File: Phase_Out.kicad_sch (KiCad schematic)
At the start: 34 parts, among them Q1 CLAMP_FET, Q2 CLAMP_FET, Q3 CLAMP_FET, Q4 CLAMP_FET, Q5 CLAMP_FET, Q6 CLAMP_FET

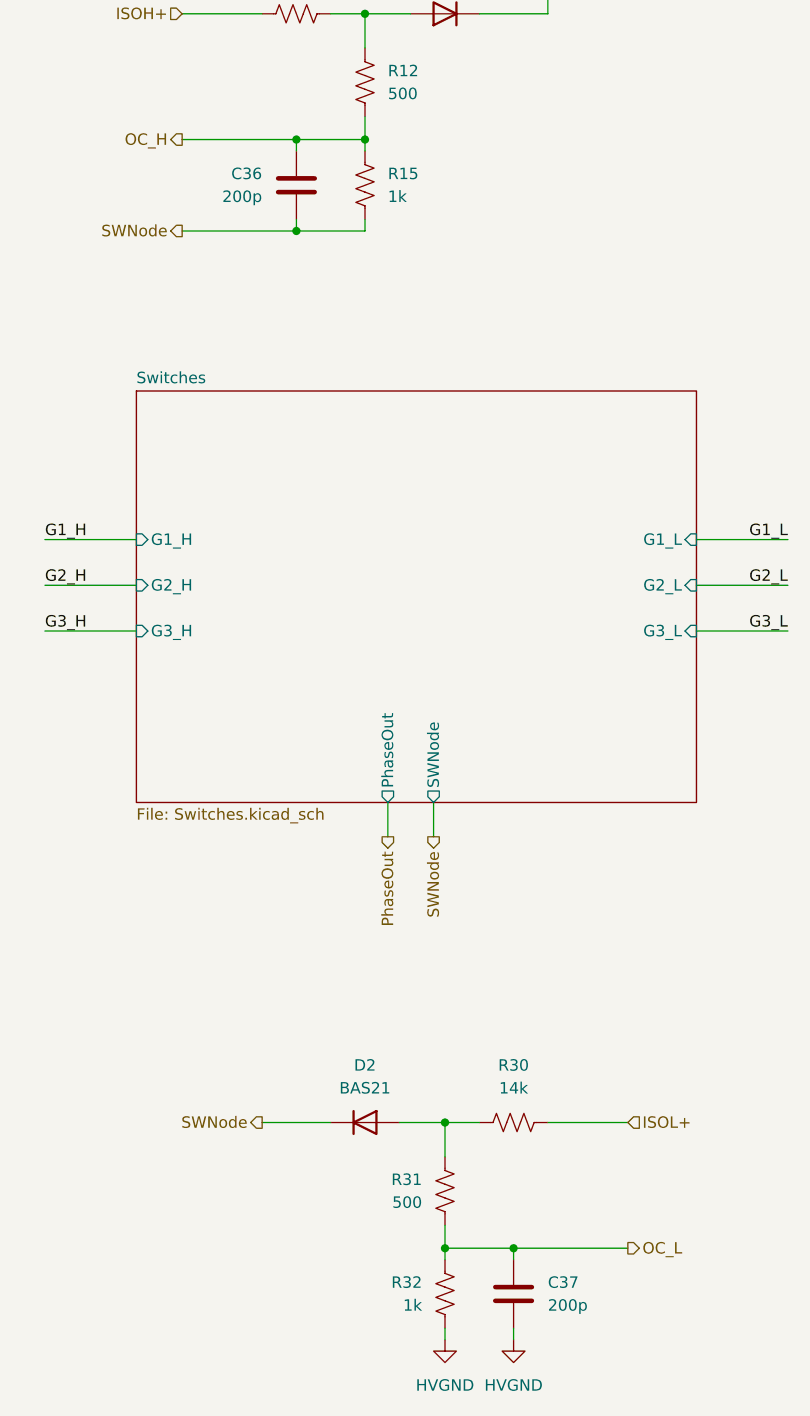
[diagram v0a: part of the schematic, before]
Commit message: new bulk caps, new HV+,- connector placement
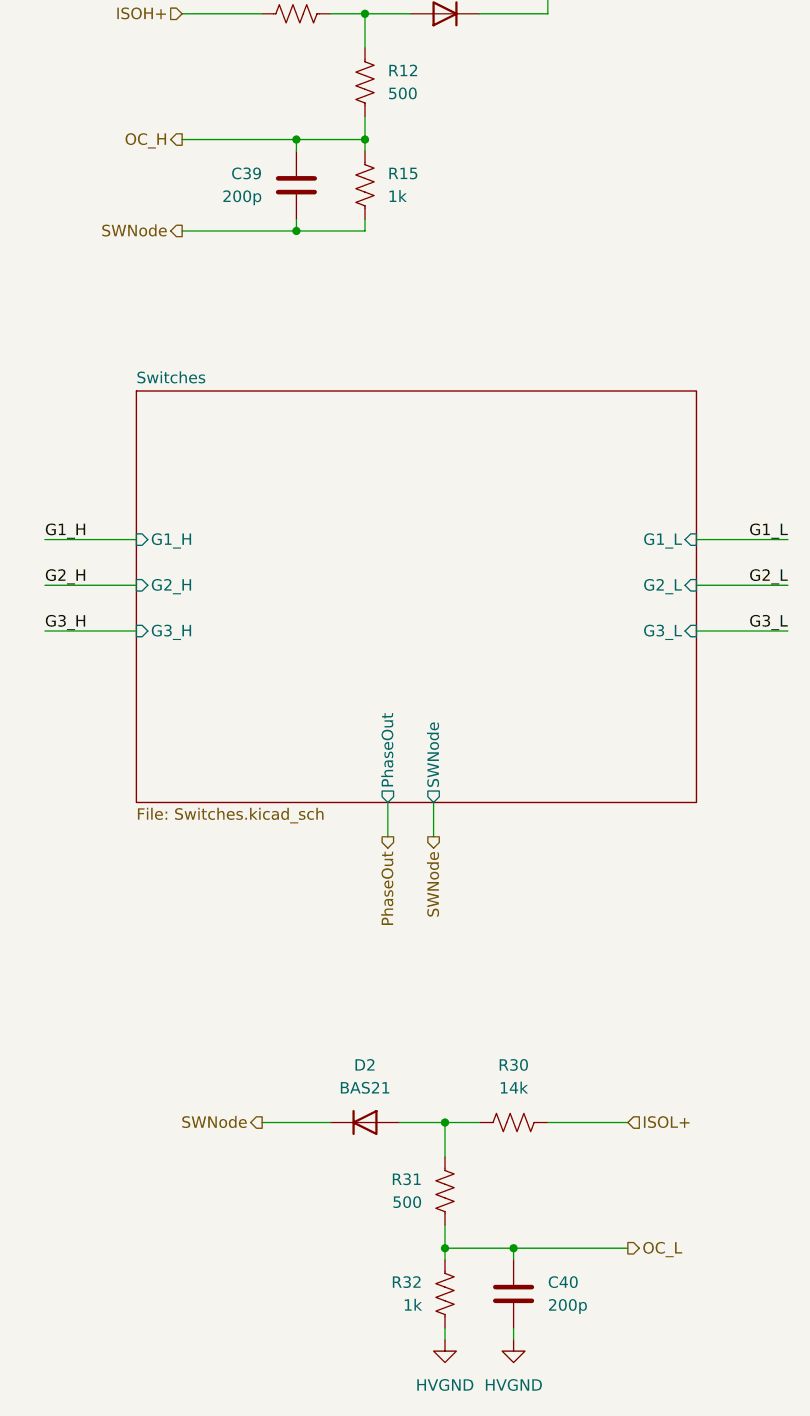
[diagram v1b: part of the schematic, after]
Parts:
- renumbered C36 to C39, C37 to C40
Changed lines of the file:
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@@
 		(dnp no)
 		(fields_autoplaced yes)
-		(property "Reference" "#PWR040"
+		(property "Reference" "#PWR046"
 			(at 157.48 179.07 0)
 			(effects
@@
 			(project "TractionInverter"
 				(path "/bc91ffbf-afc6-42bb-9d28-6a3fecc21fcc/3f7f1099-e875-4a86-860c-ef7a3936f734/8a53f8a7-4fee-45b0-8115-af4354d69d86"
-					(reference "#PWR040")
-					(unit 1)
-				)
-				(path "/bc91ffbf-afc6-42bb-9d28-6a3fecc21fcc/ebf1904e-ffdd-4ce1-98fa-2546468af80b/8a53f8a7-4fee-45b0-8115-af4354d69d86"
-					(reference "#PWR0174")
-					(unit 1)
-				)
-				(path "/bc91ffbf-afc6-42bb-9d28-6a3fecc21fcc/f1a23dc8-fe65-401e-b36f-fdc2d19203b3/8a53f8a7-4fee-45b0-8115-af4354d69d86"
-					(reference "#PWR0103")
+					(reference "#PWR046")
+					(unit 1)
+				)
+				(path "/bc91ffbf-afc6-42bb-9d28-6a3fecc21fcc/ebf1904e-ffdd-4ce1-98fa-2546468af80b/8a53f8a7-4fee-45b0-8115-af4354d69d86"
+					(reference "#PWR0162")
+					(unit 1)
+				)
+				(path "/bc91ffbf-afc6-42bb-9d28-6a3fecc21fcc/f1a23dc8-fe65-401e-b36f-fdc2d19203b3/8a53f8a7-4fee-45b0-8115-af4354d69d86"
+					(reference "#PWR097")
 					(unit 1)
 				)
@@
 		(dnp no)
 		(fields_autoplaced yes)
-		(property "Reference" "#PWR039"
+		(property "Reference" "#PWR045"
 			(at 149.86 179.07 0)
 			(effects
@@
 			(project "TractionInverter"
 				(path "/bc91ffbf-afc6-42bb-9d28-6a3fecc21fcc/3f7f1099-e875-4a86-860c-ef7a3936f734/8a53f8a7-4fee-45b0-8115-af4354d69d86"
-					(reference "#PWR039")
-					(unit 1)
-				)
-				(path "/bc91ffbf-afc6-42bb-9d28-6a3fecc21fcc/ebf1904e-ffdd-4ce1-98fa-2546468af80b/8a53f8a7-4fee-45b0-8115-af4354d69d86"
-					(reference "#PWR0173")
-					(unit 1)
-				)
-				(path "/bc91ffbf-afc6-42bb-9d28-6a3fecc21fcc/f1a23dc8-fe65-401e-b36f-fdc2d19203b3/8a53f8a7-4fee-45b0-8115-af4354d69d86"
-					(reference "#PWR0102")
+					(reference "#PWR045")
+					(unit 1)
+				)
+				(path "/bc91ffbf-afc6-42bb-9d28-6a3fecc21fcc/ebf1904e-ffdd-4ce1-98fa-2546468af80b/8a53f8a7-4fee-45b0-8115-af4354d69d86"
+					(reference "#PWR0161")
+					(unit 1)
+				)
+				(path "/bc91ffbf-afc6-42bb-9d28-6a3fecc21fcc/f1a23dc8-fe65-401e-b36f-fdc2d19203b3/8a53f8a7-4fee-45b0-8115-af4354d69d86"
+					(reference "#PWR096")
 					(unit 1)
 				)
@@
 		(on_board yes)
 		(dnp no)
-		(property "Reference" "C37"
+		(property "Reference" "C40"
 			(at 161.29 166.3699 0)
 			(effects
@@
 			(project "TractionInverter"
 				(path "/bc91ffbf-afc6-42bb-9d28-6a3fecc21fcc/3f7f1099-e875-4a86-860c-ef7a3936f734/8a53f8a7-4fee-45b0-8115-af4354d69d86"
-					(reference "C37")
-					(unit 1)
-				)
-				(path "/bc91ffbf-afc6-42bb-9d28-6a3fecc21fcc/ebf1904e-ffdd-4ce1-98fa-2546468af80b/8a53f8a7-4fee-45b0-8115-af4354d69d86"
-					(reference "C119")
-					(unit 1)
-				)
-				(path "/bc91ffbf-afc6-42bb-9d28-6a3fecc21fcc/f1a23dc8-fe65-401e-b36f-fdc2d19203b3/8a53f8a7-4fee-45b0-8115-af4354d69d86"
-					(reference "C73")
+					(reference "C40")
+					(unit 1)
+				)
+				(path "/bc91ffbf-afc6-42bb-9d28-6a3fecc21fcc/ebf1904e-ffdd-4ce1-98fa-2546468af80b/8a53f8a7-4fee-45b0-8115-af4354d69d86"
+					(reference "C122")
+					(unit 1)
+				)
+				(path "/bc91ffbf-afc6-42bb-9d28-6a3fecc21fcc/f1a23dc8-fe65-401e-b36f-fdc2d19203b3/8a53f8a7-4fee-45b0-8115-af4354d69d86"
+					(reference "C76")
 					(unit 1)
 				)
@@
 		(on_board yes)
 		(dnp no)
-		(property "Reference" "#PWR038"
+		(property "Reference" "#PWR044"
 			(at 161.29 26.67 0)
 			(effects
@@
 			(project ""
 				(path "/bc91ffbf-afc6-42bb-9d28-6a3fecc21fcc/3f7f1099-e875-4a86-860c-ef7a3936f734/8a53f8a7-4fee-45b0-8115-af4354d69d86"
-					(reference "#PWR038")
-					(unit 1)
-				)
-				(path "/bc91ffbf-afc6-42bb-9d28-6a3fecc21fcc/ebf1904e-ffdd-4ce1-98fa-2546468af80b/8a53f8a7-4fee-45b0-8115-af4354d69d86"
-					(reference "#PWR0172")
-					(unit 1)
-				)
-				(path "/bc91ffbf-afc6-42bb-9d28-6a3fecc21fcc/f1a23dc8-fe65-401e-b36f-fdc2d19203b3/8a53f8a7-4fee-45b0-8115-af4354d69d86"
-					(reference "#PWR0101")
+					(reference "#PWR044")
+					(unit 1)
+				)
+				(path "/bc91ffbf-afc6-42bb-9d28-6a3fecc21fcc/ebf1904e-ffdd-4ce1-98fa-2546468af80b/8a53f8a7-4fee-45b0-8115-af4354d69d86"
+					(reference "#PWR0160")
+					(unit 1)
+				)
+				(path "/bc91ffbf-afc6-42bb-9d28-6a3fecc21fcc/f1a23dc8-fe65-401e-b36f-fdc2d19203b3/8a53f8a7-4fee-45b0-8115-af4354d69d86"
+					(reference "#PWR095")
 					(unit 1)
 				)
@@
 		(on_board yes)
 		(dnp no)
-		(property "Reference" "C36"
+		(property "Reference" "C39"
 			(at 129.54 43.1799 0)
 			(effects
@@
 			(project "TractionInverter"
 				(path "/bc91ffbf-afc6-42bb-9d28-6a3fecc21fcc/3f7f1099-e875-4a86-860c-ef7a3936f734/8a53f8a7-4fee-45b0-8115-af4354d69d86"
-					(reference "C36")
-					(unit 1)
-				)
-				(path "/bc91ffbf-afc6-42bb-9d28-6a3fecc21fcc/ebf1904e-ffdd-4ce1-98fa-2546468af80b/8a53f8a7-4fee-45b0-8115-af4354d69d86"
-					(reference "C118")
-					(unit 1)
-				)
-				(path "/bc91ffbf-afc6-42bb-9d28-6a3fecc21fcc/f1a23dc8-fe65-401e-b36f-fdc2d19203b3/8a53f8a7-4fee-45b0-8115-af4354d69d86"
-					(reference "C72")
-					(unit 1)
-				)
+					(reference "C39")
+					(unit 1)
+				)
+				(path "/bc91ffbf-afc6-42bb-9d28-6a3fecc21fcc/ebf1904e-ffdd-4ce1-98fa-2546468af80b/8a53f8a7-4fee-45b0-8115-af4354d69d86"
+					(reference "C121")
+					(unit 1)
+				)
+				(path "/bc91ffbf-afc6-42bb-9d28-6a3fecc21fcc/f1a23dc8-fe65-401e-b36f-fdc2d19203b3/8a53f8a7-4fee-45b0-8115-af4354d69d86"
+					(reference "C75")
+					(unit 1)
+				)

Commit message: killed testpoints
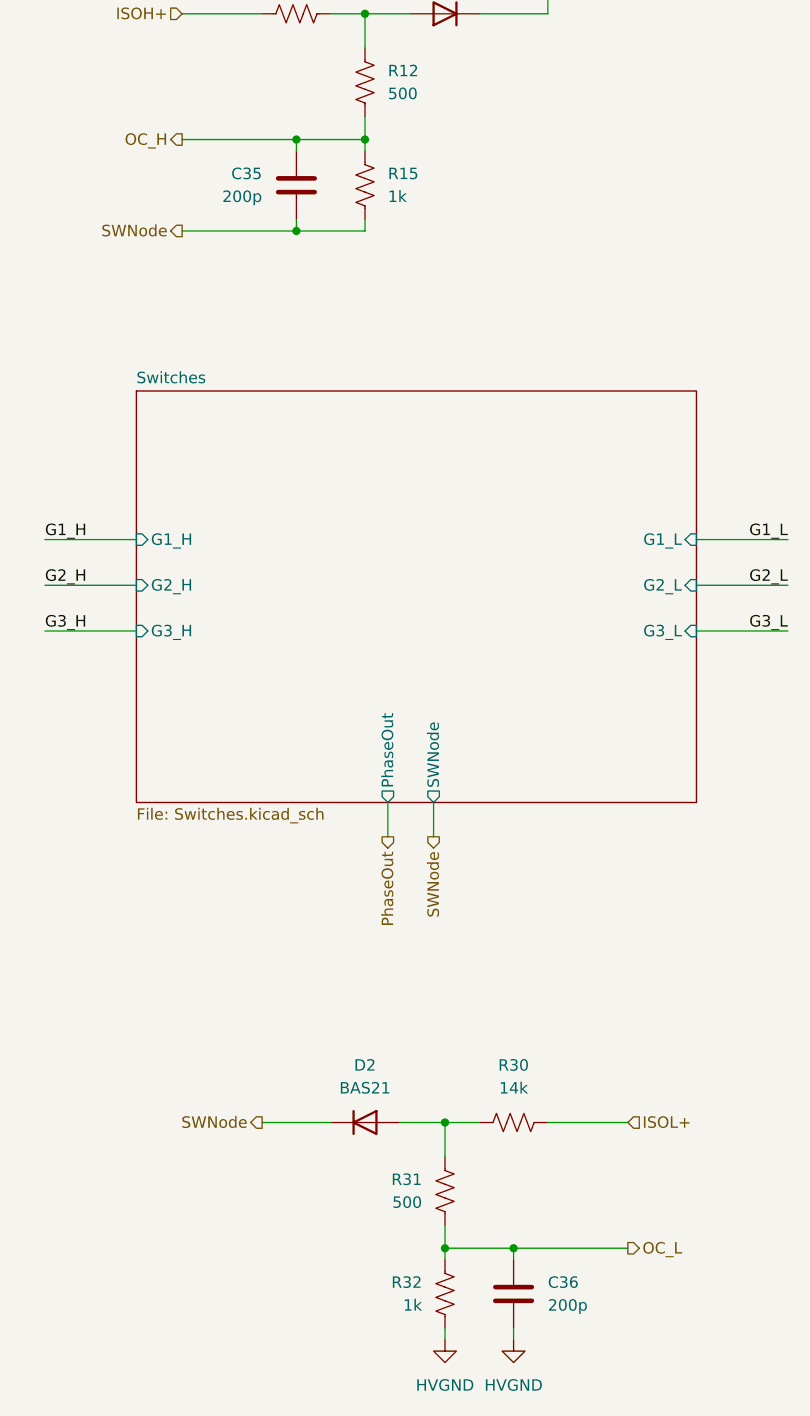
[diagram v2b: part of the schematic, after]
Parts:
- renumbered C39 to C35, C40 to C36
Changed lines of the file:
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@@
 		(dnp no)
 		(fields_autoplaced yes)
-		(property "Reference" "#PWR046"
+		(property "Reference" "#PWR038"
 			(at 157.48 179.07 0)
 			(effects
@@
 			(project "TractionInverter"
 				(path "/bc91ffbf-afc6-42bb-9d28-6a3fecc21fcc/3f7f1099-e875-4a86-860c-ef7a3936f734/8a53f8a7-4fee-45b0-8115-af4354d69d86"
-					(reference "#PWR046")
-					(unit 1)
-				)
-				(path "/bc91ffbf-afc6-42bb-9d28-6a3fecc21fcc/ebf1904e-ffdd-4ce1-98fa-2546468af80b/8a53f8a7-4fee-45b0-8115-af4354d69d86"
-					(reference "#PWR0162")
-					(unit 1)
-				)
-				(path "/bc91ffbf-afc6-42bb-9d28-6a3fecc21fcc/f1a23dc8-fe65-401e-b36f-fdc2d19203b3/8a53f8a7-4fee-45b0-8115-af4354d69d86"
-					(reference "#PWR097")
+					(reference "#PWR038")
+					(unit 1)
+				)
+				(path "/bc91ffbf-afc6-42bb-9d28-6a3fecc21fcc/ebf1904e-ffdd-4ce1-98fa-2546468af80b/8a53f8a7-4fee-45b0-8115-af4354d69d86"
+					(reference "#PWR0154")
+					(unit 1)
+				)
+				(path "/bc91ffbf-afc6-42bb-9d28-6a3fecc21fcc/f1a23dc8-fe65-401e-b36f-fdc2d19203b3/8a53f8a7-4fee-45b0-8115-af4354d69d86"
+					(reference "#PWR089")
 					(unit 1)
 				)
@@
 		(dnp no)
 		(fields_autoplaced yes)
-		(property "Reference" "#PWR045"
+		(property "Reference" "#PWR037"
 			(at 149.86 179.07 0)
 			(effects
@@
 			(project "TractionInverter"
 				(path "/bc91ffbf-afc6-42bb-9d28-6a3fecc21fcc/3f7f1099-e875-4a86-860c-ef7a3936f734/8a53f8a7-4fee-45b0-8115-af4354d69d86"
-					(reference "#PWR045")
-					(unit 1)
-				)
-				(path "/bc91ffbf-afc6-42bb-9d28-6a3fecc21fcc/ebf1904e-ffdd-4ce1-98fa-2546468af80b/8a53f8a7-4fee-45b0-8115-af4354d69d86"
-					(reference "#PWR0161")
-					(unit 1)
-				)
-				(path "/bc91ffbf-afc6-42bb-9d28-6a3fecc21fcc/f1a23dc8-fe65-401e-b36f-fdc2d19203b3/8a53f8a7-4fee-45b0-8115-af4354d69d86"
-					(reference "#PWR096")
+					(reference "#PWR037")
+					(unit 1)
+				)
+				(path "/bc91ffbf-afc6-42bb-9d28-6a3fecc21fcc/ebf1904e-ffdd-4ce1-98fa-2546468af80b/8a53f8a7-4fee-45b0-8115-af4354d69d86"
+					(reference "#PWR0153")
+					(unit 1)
+				)
+				(path "/bc91ffbf-afc6-42bb-9d28-6a3fecc21fcc/f1a23dc8-fe65-401e-b36f-fdc2d19203b3/8a53f8a7-4fee-45b0-8115-af4354d69d86"
+					(reference "#PWR088")
 					(unit 1)
 				)
@@
 		(on_board yes)
 		(dnp no)
-		(property "Reference" "C40"
+		(property "Reference" "C36"
 			(at 161.29 166.3699 0)
 			(effects
@@
 			(project "TractionInverter"
 				(path "/bc91ffbf-afc6-42bb-9d28-6a3fecc21fcc/3f7f1099-e875-4a86-860c-ef7a3936f734/8a53f8a7-4fee-45b0-8115-af4354d69d86"
-					(reference "C40")
-					(unit 1)
-				)
-				(path "/bc91ffbf-afc6-42bb-9d28-6a3fecc21fcc/ebf1904e-ffdd-4ce1-98fa-2546468af80b/8a53f8a7-4fee-45b0-8115-af4354d69d86"
-					(reference "C122")
-					(unit 1)
-				)
-				(path "/bc91ffbf-afc6-42bb-9d28-6a3fecc21fcc/f1a23dc8-fe65-401e-b36f-fdc2d19203b3/8a53f8a7-4fee-45b0-8115-af4354d69d86"
-					(reference "C76")
+					(reference "C36")
+					(unit 1)
+				)
+				(path "/bc91ffbf-afc6-42bb-9d28-6a3fecc21fcc/ebf1904e-ffdd-4ce1-98fa-2546468af80b/8a53f8a7-4fee-45b0-8115-af4354d69d86"
+					(reference "C118")
+					(unit 1)
+				)
+				(path "/bc91ffbf-afc6-42bb-9d28-6a3fecc21fcc/f1a23dc8-fe65-401e-b36f-fdc2d19203b3/8a53f8a7-4fee-45b0-8115-af4354d69d86"
+					(reference "C72")
 					(unit 1)
 				)
@@
 		(on_board yes)
 		(dnp no)
-		(property "Reference" "#PWR044"
+		(property "Reference" "#PWR036"
 			(at 161.29 26.67 0)
 			(effects
@@
 			(project ""
 				(path "/bc91ffbf-afc6-42bb-9d28-6a3fecc21fcc/3f7f1099-e875-4a86-860c-ef7a3936f734/8a53f8a7-4fee-45b0-8115-af4354d69d86"
-					(reference "#PWR044")
-					(unit 1)
-				)
-				(path "/bc91ffbf-afc6-42bb-9d28-6a3fecc21fcc/ebf1904e-ffdd-4ce1-98fa-2546468af80b/8a53f8a7-4fee-45b0-8115-af4354d69d86"
-					(reference "#PWR0160")
-					(unit 1)
-				)
-				(path "/bc91ffbf-afc6-42bb-9d28-6a3fecc21fcc/f1a23dc8-fe65-401e-b36f-fdc2d19203b3/8a53f8a7-4fee-45b0-8115-af4354d69d86"
-					(reference "#PWR095")
+					(reference "#PWR036")
+					(unit 1)
+				)
+				(path "/bc91ffbf-afc6-42bb-9d28-6a3fecc21fcc/ebf1904e-ffdd-4ce1-98fa-2546468af80b/8a53f8a7-4fee-45b0-8115-af4354d69d86"
+					(reference "#PWR0152")
+					(unit 1)
+				)
+				(path "/bc91ffbf-afc6-42bb-9d28-6a3fecc21fcc/f1a23dc8-fe65-401e-b36f-fdc2d19203b3/8a53f8a7-4fee-45b0-8115-af4354d69d86"
+					(reference "#PWR087")
 					(unit 1)
 				)
@@
 		(on_board yes)
 		(dnp no)
-		(property "Reference" "C39"
+		(property "Reference" "C35"
 			(at 129.54 43.1799 0)
 			(effects
@@
 			(project "TractionInverter"
 				(path "/bc91ffbf-afc6-42bb-9d28-6a3fecc21fcc/3f7f1099-e875-4a86-860c-ef7a3936f734/8a53f8a7-4fee-45b0-8115-af4354d69d86"
-					(reference "C39")
-					(unit 1)
-				)
-				(path "/bc91ffbf-afc6-42bb-9d28-6a3fecc21fcc/ebf1904e-ffdd-4ce1-98fa-2546468af80b/8a53f8a7-4fee-45b0-8115-af4354d69d86"
-					(reference "C121")
-					(unit 1)
-				)
-				(path "/bc91ffbf-afc6-42bb-9d28-6a3fecc21fcc/f1a23dc8-fe65-401e-b36f-fdc2d19203b3/8a53f8a7-4fee-45b0-8115-af4354d69d86"
-					(reference "C75")
-					(unit 1)
-				)
+					(reference "C35")
+					(unit 1)
+				)
+				(path "/bc91ffbf-afc6-42bb-9d28-6a3fecc21fcc/ebf1904e-ffdd-4ce1-98fa-2546468af80b/8a53f8a7-4fee-45b0-8115-af4354d69d86"
+					(reference "C117")
+					(unit 1)
+				)
+				(path "/bc91ffbf-afc6-42bb-9d28-6a3fecc21fcc/f1a23dc8-fe65-401e-b36f-fdc2d19203b3/8a53f8a7-4fee-45b0-8115-af4354d69d86"
+					(reference "C71")
+					(unit 1)
+				)
